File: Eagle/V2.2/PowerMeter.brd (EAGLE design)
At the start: 100 x 80 mm, 56 parts, among them IC1 74HC138D, IC2 4052D, IC3 CS5463, Q1 4.096MHz, T1 TV16E, T2 TV16E, T3 TV16E, X1 RASPI_BOARD_B+_E4

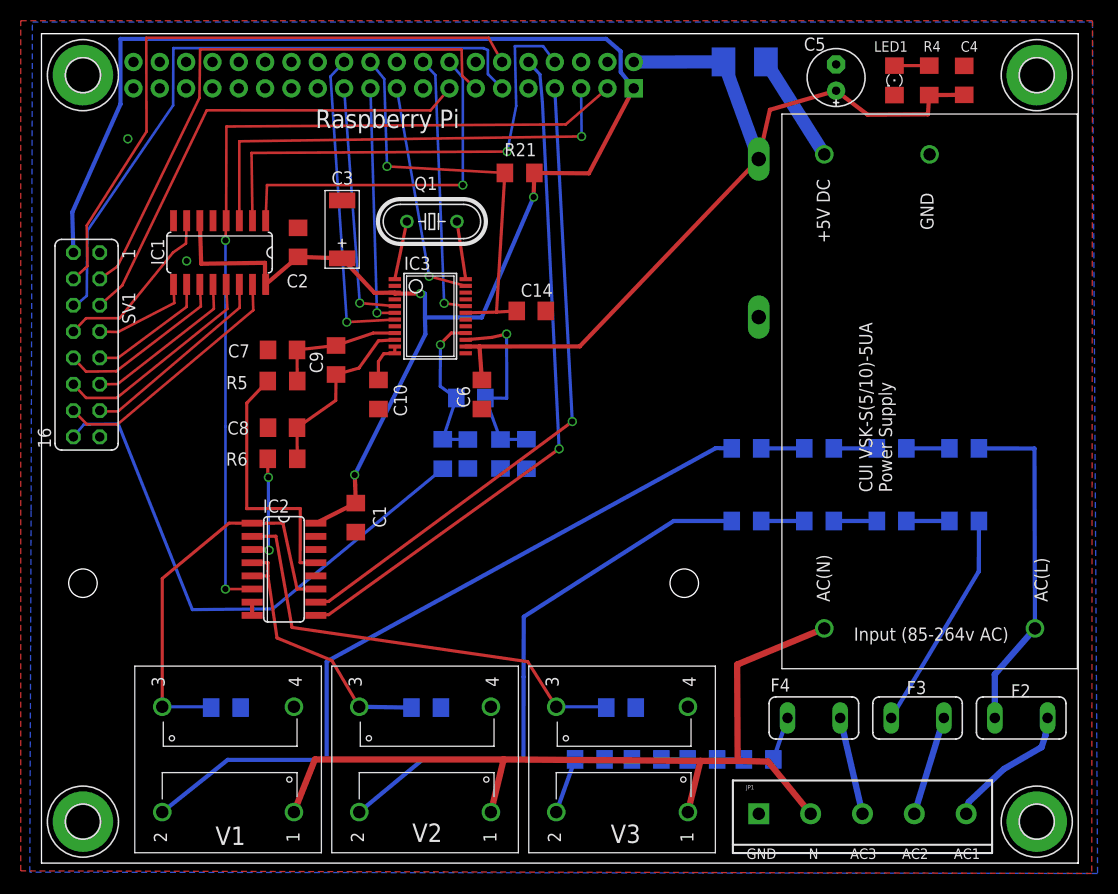
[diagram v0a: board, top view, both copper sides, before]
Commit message: Cleaned up some thing
cleaned up traces, made 3.5mm connectors, caps & diode SMD, put everything on same side of boards (may need to put resistor arrays back on the underside of the main board).
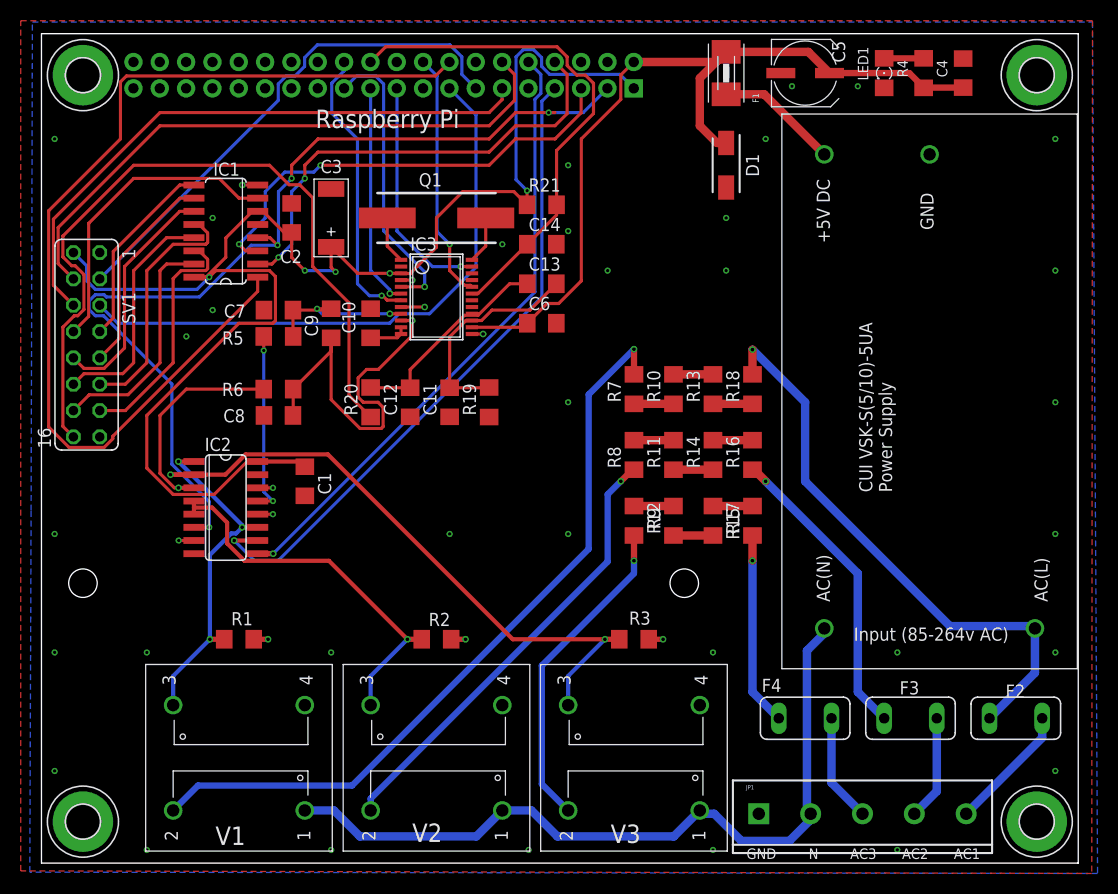
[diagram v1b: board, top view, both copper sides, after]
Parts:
- C5: value 220uF -> 220uF / 865080345012; device adafruit:E2,5-6E -> rcl:UD-6,3X7,7_NICHICON
- D1: value P6KE6.8A -> SMBJP6KE6.8A-TP; device diode:C1702-15 -> SamacSys_Parts:DIOM5226X240N
- Q1: device crystal:HC49/S -> SamacSys_Parts:SMD-HC-49-S
- moved R9 23.4 mm to (57.1, 33.0), flipped to the top, turned to 270 degrees
- moved R12 23.2 mm to (61.0, 33.0), flipped to the top, turned to 90 degrees
- moved R15 23.0 mm to (64.8, 33.0), flipped to the top, turned to 270 degrees
- moved R17 23.0 mm to (68.6, 33.0), flipped to the top, turned to 90 degrees
- moved R16 21.4 mm to (68.6, 39.4), flipped to the top, turned to 90 degrees
- moved R18 21.2 mm to (68.6, 45.7), flipped to the top, turned to 270 degrees
- moved R14 18.4 mm to (64.8, 39.4), flipped to the top, turned to 270 degrees
- moved R13 18.2 mm to (64.8, 45.7), flipped to the top, turned to 90 degrees
- moved R11 15.4 mm to (61.0, 39.4), flipped to the top, turned to 90 degrees
- moved R10 15.2 mm to (61.0, 45.7), flipped to the top, turned to 270 degrees
- moved C13 13.0 mm to (48.3, 55.9), flipped to the top, turned to 0 degrees
- moved R8 12.6 mm to (57.1, 39.4), flipped to the top, turned to 270 degrees
- moved R7 12.3 mm to (57.1, 45.7), flipped to the top, turned to 90 degrees
- moved C6 8.98 mm to (48.3, 52.1), turned to 180 degrees
- moved R20 8.56 mm to (31.8, 44.5), flipped to the top
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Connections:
- net 5V: now also D1.1; no longer D1.C
- net GND: now also D1.2; no longer D1.A
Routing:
- net BS-A: track 34.7 -> 97.4 mm, vias 1 -> 0
- net N$11: track 5.40 -> 31.3 mm, vias 0 -> 1
- net AC(L): track 32.8 -> 55.7 mm, vias 0 -> 1
- net +3V3: track 167.2 -> 145.5 mm, vias 3 -> 5
- net IIN+: track 53.2 -> 73.6 mm
- net N$46: track 17.2 -> 37.2 mm, vias 0 -> 1
- net VIN-3: track 44.3 -> 61.6 mm, vias 0 -> 2
- net N$21: track 4.23 -> 18.7 mm, vias 0 -> 1
- net GND: track 1.27 -> 14.5 mm, vias 2 -> 44
- net BS-7: track 16.9 -> 29.9 mm
- net VIN-2: track 26.3 -> 38.8 mm, vias 0 -> 1
- net CS-D: track 46.0 -> 57.6 mm
- net N$39: track 10.7 -> 22.0 mm, vias 2 -> 1
- net N$15: track 54.2 -> 43.5 mm, vias 0 -> 1
- net AC(N): track 84.4 -> 74.3 mm
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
